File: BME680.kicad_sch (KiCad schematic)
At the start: 19 parts, among them IC1 BME680, J1 HEADER-1X770MIL, Q2 BSS138, U2 AP2112K-3.3

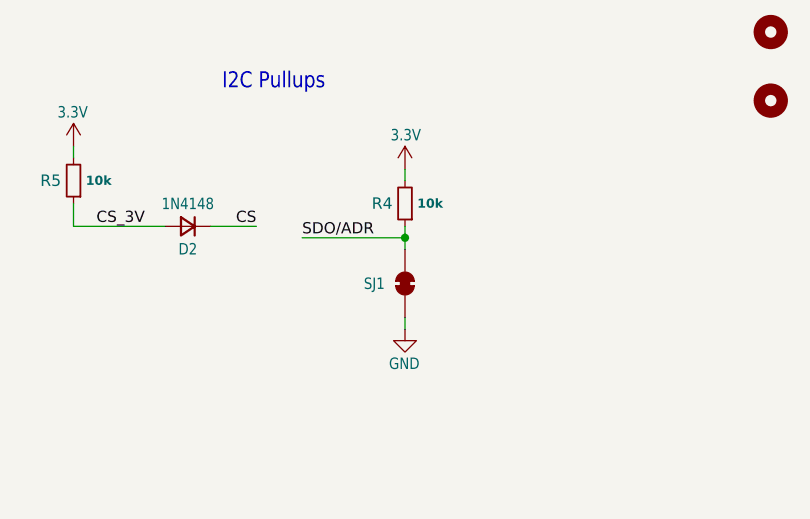
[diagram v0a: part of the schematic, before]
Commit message: solder jumper fix
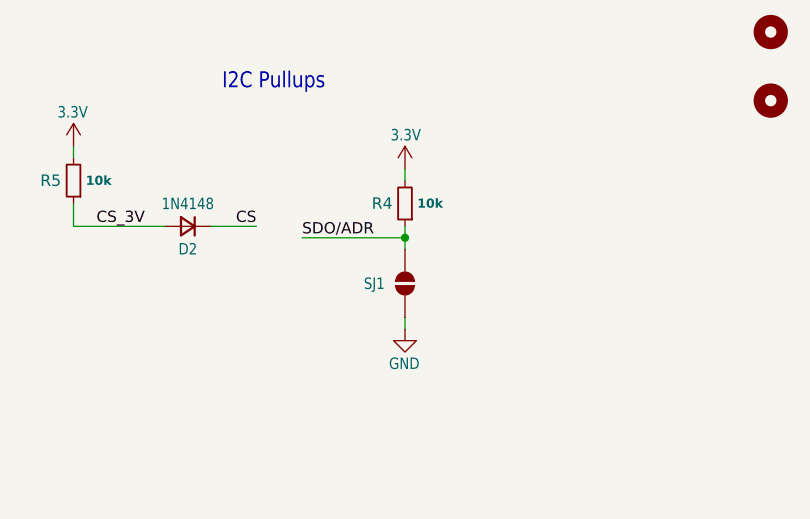
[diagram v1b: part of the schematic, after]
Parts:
- SJ1: symbol Jumper:SolderJumper_2_Bridged -> Jumper:SolderJumper_2_Open
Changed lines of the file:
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@@
 			)
 		)
-		(property "Datasheet" "~"
+		(property "Datasheet" ""
 			(at 240.03 110.49 0)
 			(effects
@@
 			)
 		)
-		(property "Datasheet" "~"
+		(property "Datasheet" ""
 			(at 204.47 66.04 0)
 			(effects
@@
 			)
 		)
-		(property "Datasheet" "~"
+		(property "Datasheet" ""
 			(at 40.64 69.85 0)
 			(effects
@@
 			)
 		)
-		(property "Datasheet" "https://www.diodes.com/assets/Datasheets/AP2112.pdf"
+		(property "Datasheet" ""
 			(at 63.5 63.5 0)
 			(effects
@@
 			)
 		)
-		(property "Datasheet" "~"
+		(property "Datasheet" ""
 			(at 199.39 129.54 0)
 			(effects
@@
 			)
 		)
-		(property "Datasheet" "~"
+		(property "Datasheet" ""
 			(at 196.85 66.04 0)
 			(effects
@@
 			)
 		)
-		(property "Datasheet" "~"
+		(property "Datasheet" ""
 			(at 186.69 78.74 0)
 			(effects
@@
 			)
 		)
-		(property "Datasheet" "~"
+		(property "Datasheet" ""
 			(at 118.11 66.04 0)
 			(effects
@@
 			)
 		)
-		(property "Datasheet" "~"
+		(property "Datasheet" ""
 			(at 179.07 88.9 0)
 			(effects
@@
 			)
 		)
-		(property "Datasheet" "~"
+		(property "Datasheet" ""
 			(at 175.26 132.08 90)
 			(effects
@@
 			)
 		)
-		(property "Datasheet" "~"
+		(property "Datasheet" ""
 			(at 240.03 118.11 0)
 			(effects
@@
 			)
 		)
-		(property "Datasheet" "~"
+		(property "Datasheet" ""
 			(at 162.56 127 0)
 			(effects
@@
 			)
 		)
-		(property "Datasheet" "~"
+		(property "Datasheet" ""
 			(at 161.29 66.04 0)
 			(effects
@@
 			)
 		)
-		(property "Datasheet" "~"
+		(property "Datasheet" ""
 			(at 74.93 130.81 0)
 			(effects
@@
 	)
 	(symbol
-		(lib_id "Jumper:SolderJumper_2_Bridged")
+		(lib_id "Jumper:SolderJumper_2_Open")
 		(at 199.39 138.43 270)
 		(unit 1)
@@
 			)
 		)
-		(property "Datasheet" "~"
+		(property "Datasheet" ""
 			(at 199.39 138.43 0)
 			(effects
@@
 			)
 		)
-		(property "Description" "Solder Jumper, 2-pole, closed/bridged"
+		(property "Description" "Solder Jumper, 2-pole, open"
 			(at 199.39 138.43 0)
 			(effects
@@
 			)
 		)
-		(property "Datasheet" "~"
+		(property "Datasheet" ""
 			(at 168.91 66.04 0)
 			(effects
@@
 			)
 		)
-		(property "Datasheet" "~"
+		(property "Datasheet" ""
 			(at 81.28 68.58 0)
 			(effects
@@
 			)
 		)
-		(property "Datasheet" "~"
+		(property "Datasheet" ""
 			(at 118.11 76.2 90)
 			(effects
@@
 			)
 		)
-		(property "Datasheet" "~"
+		(property "Datasheet" ""
 			(at 91.44 68.58 0)
 			(effects
@@
 			)
 		)
-		(property "Datasheet" "https://ae-bst.resource.bosch.com/media/_tech/media/datasheets/BST-BME680-DS001.pdf"
+		(property "Datasheet" ""
 			(at 113.03 135.89 0)
 			(effects

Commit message: BOM presets update
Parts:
- C1: Componant package type C_0603 -> (none)
- C2, C3: Componant package type C_0805 -> (none)
- D1: Componant package type LED_0603 -> (none)
- D2: Componant package type SOD-323 -> (none)
- IC1, J1: Componant package type / -> (none)
- Q2: Componant package type SOT-363 -> (none)
- R1, R2, R3, R4, R5, R6, R7: Componant package type R_0603 -> (none)
- U2: Componant package type SOT-25 -> (none)
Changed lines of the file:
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@@
 			)
 		)
-		(property "Componant package type" ""
-			(at 240.03 110.49 0)
-			(effects
-				(font
-					(size 1.27 1.27)
-				)
-				(hide yes)
-			)
-		)
 		(property "MPN" ""
 			(at 240.03 110.49 0)
@@
 			)
 		)
-		(property "Componant package type" "R_0603"
-			(at 204.47 66.04 0)
-			(effects
-				(font
-					(size 1.27 1.27)
-				)
-				(hide yes)
-			)
-		)
 		(property "MPN" "/"
 			(at 204.47 66.04 0)
@@
 			)
 		)
-		(property "Componant package type" "C_0805"
-			(at 40.64 69.85 0)
-			(effects
-				(font
-					(size 1.27 1.27)
-				)
-				(hide yes)
-			)
-		)
 		(property "MPN" "/"
 			(at 40.64 69.85 0)
@@
 			)
 		)
-		(property "Componant package type" "SOT-25"
-			(at 63.5 66.04 0)
-			(effects
-				(font
-					(size 1.27 1.27)
-				)
-				(hide yes)
-			)
-		)
 		(property "MPN" "AP2112K-3.3TRG1"
 			(at 63.5 66.04 0)
@@
 			)
 		)
-		(property "Componant package type" "R_0603"
-			(at 199.39 129.54 0)
-			(effects
-				(font
-					(size 1.27 1.27)
-				)
-				(hide yes)
-			)
-		)
 		(property "MPN" "/"
 			(at 199.39 129.54 0)
@@
 			)
 		)
-		(property "Componant package type" "R_0603"
-			(at 196.85 66.04 0)
-			(effects
-				(font
-					(size 1.27 1.27)
-				)
-				(hide yes)
-			)
-		)
 		(property "MPN" "/"
 			(at 196.85 66.04 0)
@@
 			)
 		)
-		(property "Componant package type" "SOT-363"
-			(at 186.69 73.66 0)
-			(effects
-				(font
-					(size 1.27 1.27)
-				)
-				(hide yes)
-			)
-		)
 		(property "MPN" "BSS138DWQ-7"
 			(at 186.69 73.66 0)
@@
 			)
 		)
-		(property "Componant package type" "R_0603"
-			(at 118.11 66.04 0)
-			(effects
-				(font
-					(size 1.27 1.27)
-				)
-				(hide yes)
-			)
-		)
 		(property "MPN" "/"
 			(at 118.11 66.04 0)
@@
 			)
 		)
-		(property "Componant package type" "SOT-363"
-			(at 179.07 83.82 0)
-			(effects
-				(font
-					(size 1.27 1.27)
-				)
-				(hide yes)
-			)
-		)
 		(property "MPN" "BSS138DWQ-7"
 			(at 179.07 83.82 0)
@@
 			)
 		)
-		(property "Componant package type" "SOD-323"
-			(at 175.26 132.08 0)
-			(effects
-				(font
-					(size 1.27 1.27)
-				)
-				(hide yes)
-			)
-		)
 		(property "MPN" "1N4148WX-TP"
 			(at 175.26 132.08 0)
@@
 			)
 		)
-		(property "Componant package type" ""
-			(at 240.03 118.11 0)
-			(effects
-				(font
-					(size 1.27 1.27)
-				)
-				(hide yes)
-			)
-		)
 		(property "MPN" ""
 			(at 240.03 118.11 0)
@@
 			)
 		)
-		(property "Componant package type" "R_0603"
-			(at 162.56 127 0)
-			(effects
-				(font
-					(size 1.27 1.27)
-				)
-				(hide yes)
-			)
-		)
 		(property "MPN" "/"
 			(at 162.56 127 0)
@@
 			)
 		)
-		(property "Componant package type" "R_0603"
-			(at 161.29 66.04 0)
-			(effects
-				(font
-					(size 1.27 1.27)
-				)
-				(hide yes)
-			)
-		)
 		(property "MPN" "/"
 			(at 161.29 66.04 0)
@@
 			)
 		)
-		(property "Componant package type" "/"
-			(at 74.93 130.81 0)
-			(effects
-				(font
-					(size 1.27 1.27)
-				)
-				(hide yes)
-			)
-		)
 		(property "MPN" "TSW-107-23-G-S"
 			(at 74.93 130.81 0)
@@
 			)
 		)
-		(property "Componant package type" ""
-			(at 199.39 138.43 0)
-			(effects
-				(font
-					(size 1.27 1.27)
-				)
-				(hide yes)
-			)
-		)
 		(property "MPN" ""
 			(at 199.39 138.43 0)
@@
 			)
 		)
-		(property "Componant package type" "R_0603"
-			(at 168.91 66.04 0)
-			(effects
-				(font
-					(size 1.27 1.27)
-				)
-				(hide yes)
-			)
-		)
 		(property "MPN" "/"
 			(at 168.91 66.04 0)
@@
 			)
 		)
-		(property "Componant package type" "C_0805"
-			(at 81.28 68.58 0)
-			(effects
-				(font
-					(size 1.27 1.27)
-				)
-				(hide yes)
-			)
-		)
 		(property "MPN" "/"
 			(at 81.28 68.58 0)
@@
 			)
 		)
-		(property "Componant package type" "LED_0603"
-			(at 118.11 76.2 0)
-			(effects
-				(font
-					(size 1.27 1.27)
-				)
-				(hide yes)
-			)
-		)
 		(property "MPN" "150060GS75000"
 			(at 118.11 76.2 0)
@@
 			)
 		)
-		(property "Componant package type" "C_0603"
-			(at 91.44 68.58 0)
-			(effects
-				(font
-					(size 1.27 1.27)
-				)
-				(hide yes)
-			)
-		)
 		(property "MPN" "/"
 			(at 91.44 68.58 0)
@@
 			(at 113.03 130.81 0)
 			(effects
-				(font
-					(size 1.27 1.27)
-				)
-				(hide yes)
-			)
-		)
-		(property "Componant package type" "/"
-			(at 113.03 130.81 0)
-			(effects
